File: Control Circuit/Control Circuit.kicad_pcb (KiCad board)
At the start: 2 copper layers, 126 x 125.5 mm, 7 parts, among them U1 Adafruit DPS310, U3 Adafruit BNO085, U4 TPS61087

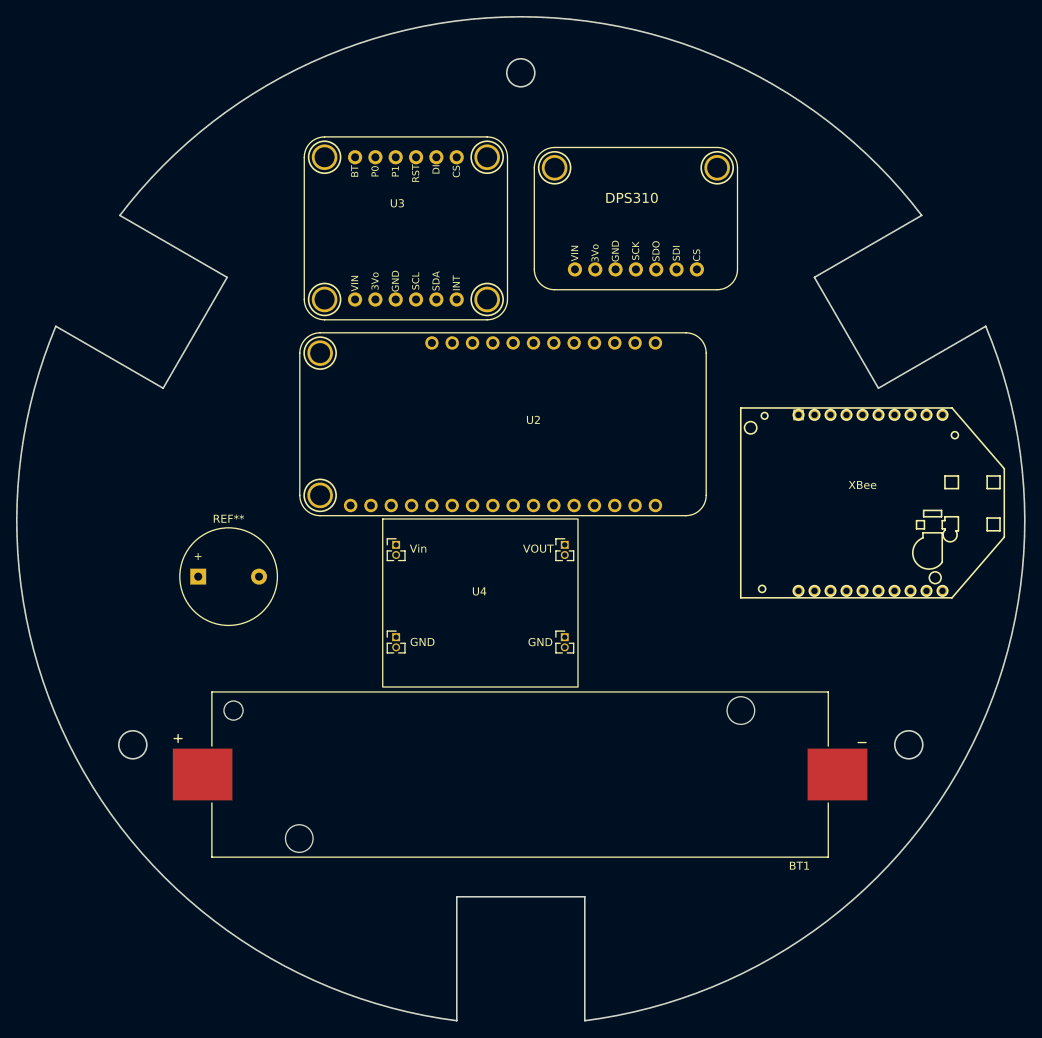
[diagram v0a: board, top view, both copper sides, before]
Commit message: switching from development board to on board chip
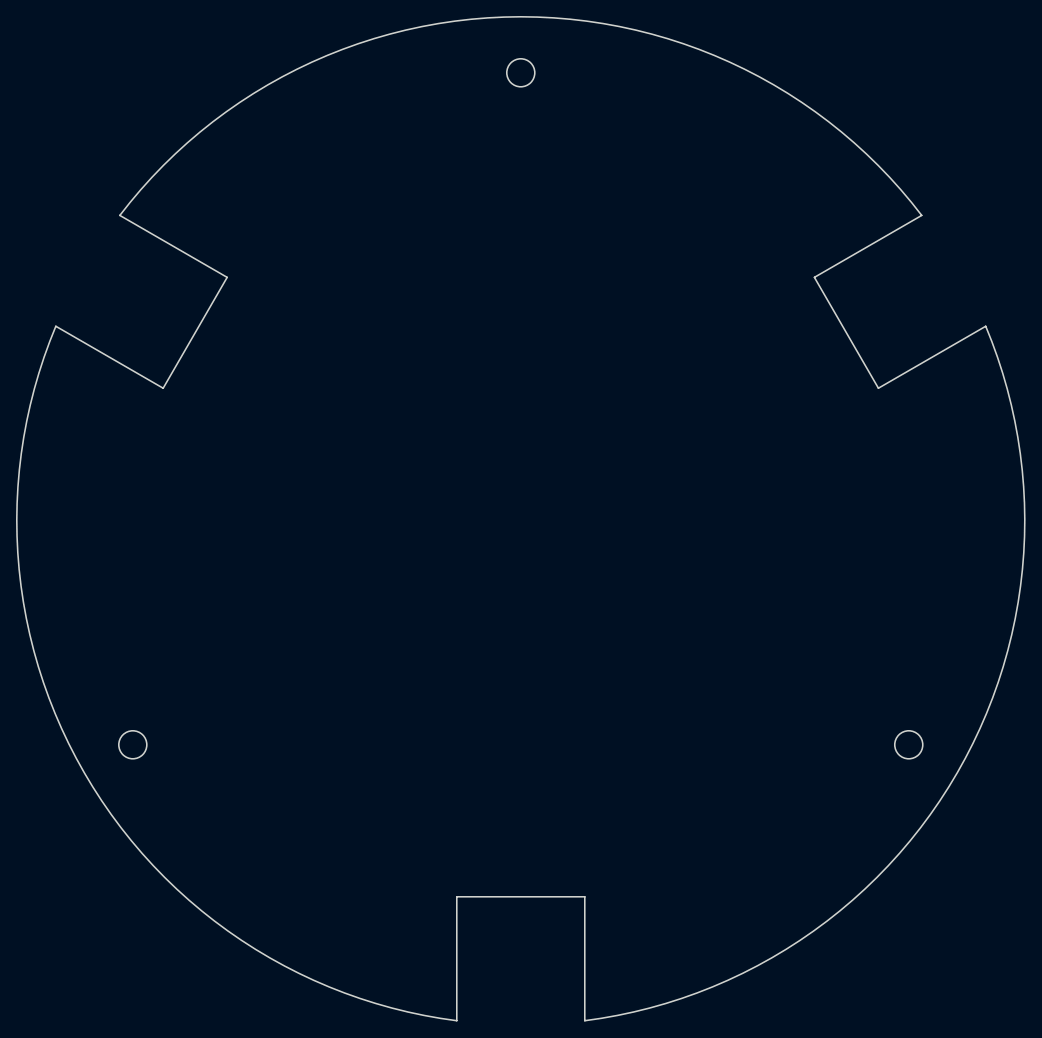
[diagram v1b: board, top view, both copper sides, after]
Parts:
- removed BT1: 18650 Cell holder, 18650 Cell Holder:18560 holder
- removed REF**: Buzzer_12x9.5RM7.6, Buzzer_Beeper:Buzzer_12x9.5RM7.6
- removed U1: Adafruit DPS310, DPS310:Adafruit DPS310
- removed U2: ~, STM32F405:Adafruit Feather STM32F405 Express
- removed U3: Adafruit BNO085, BNO085:Adafruit BNO085
- removed U4: TPS61087, Boost Converter:TPS61087 Breakout
- removed XBee: Digi XBee, Digi XBee:Digi XBee
